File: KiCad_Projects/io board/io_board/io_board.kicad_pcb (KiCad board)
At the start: 2 copper layers, 78.4 x 100.1 mm, 15 parts, among them J1 Conn_01x13_Female, SW1 SW_Push, SW2 SW_Push, SW3 SW_Push, SW4 SW_Push, SW5 SW_DIP_x01, U1 LCD_Module

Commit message: 基盤データのアップデート
ローカルコミットはちゃんと作ってください
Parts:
- turned SW5 to -90 degrees
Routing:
- net GND1: track 49.0 -> 38.2 mm
- net +7.5V: track 45.2 -> 46.8 mm
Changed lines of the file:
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@@
   )
   (footprint "Lib:DS-850k" (layer "F.Cu")
-    (at 179.324 72.644 90)
+    (at 179.324 72.644 -90)
     (property "Sheetfile" "io_board.kicad_sch")
     (property "Sheetname" "")
@@
     (fp_line (start -10.5 -7.5) (end -10.5 7.5) (layer "F.SilkS") (width 0.12))
     (fp_line (start -7.5 4.7) (end 7.5 4.7) (layer "F.SilkS") (width 0.12))
-    (pad "1" thru_hole oval locked (at 0 0 180) (size 4 2) (drill oval 3 1) (layers *.Cu *.Mask)
+    (pad "1" thru_hole oval locked (at 0 0) (size 4 2) (drill oval 3 1) (layers *.Cu *.Mask)
       (net 13 "+7.5V") (pintype "passive"))
-    (pad "2" thru_hole oval locked (at -6 0 180) (size 4 2) (drill oval 3 1) (layers *.Cu *.Mask)
+    (pad "2" thru_hole oval locked (at -6 0) (size 4 2) (drill oval 3 1) (layers *.Cu *.Mask)
       (net 12 "GND1") (pintype "passive"))
   )
@@
   (segment (start 163.576 61.976) (end 169.672 68.072) (width 0.25) (layer "B.Cu") (net 11))
   (segment (start 141.239 54.879) (end 148.336 61.976) (width 0.25) (layer "B.Cu") (net 11))
-  (segment (start 153.939 52.817) (end 153.939 50.267) (width 2) (layer "B.Cu") (net 12))
-  (segment (start 172.292 71.612) (end 172.292 53.892978) (width 2) (layer "B.Cu") (net 12))
-  (segment (start 153.924 52.832) (end 153.939 52.817) (width 2) (layer "B.Cu") (net 12))
-  (segment (start 171.231022 52.832) (end 153.924 52.832) (width 2) (layer "B.Cu") (net 12))
-  (segment (start 179.324 78.644) (end 172.292 71.612) (width 2) (layer "B.Cu") (net 12))
-  (segment (start 172.292 53.892978) (end 171.231022 52.832) (width 2) (layer "B.Cu") (net 12))
-  (segment (start 179.299 50.267) (end 156.479 50.267) (width 2) (layer "B.Cu") (net 13))
-  (segment (start 179.324 72.644) (end 179.324 50.292) (width 2) (layer "B.Cu") (net 13))
-  (segment (start 179.324 50.292) (end 179.299 50.267) (width 2) (layer "B.Cu") (net 13))
+  (segment (start 154.686 52.832) (end 173.99 52.832) (width 2) (layer "B.Cu") (net 12))
+  (segment (start 153.939 52.085) (end 154.686 52.832) (width 2) (layer "B.Cu") (net 12))
+  (segment (start 153.939 50.267) (end 153.939 52.085) (width 2) (layer "B.Cu") (net 12))
+  (segment (start 179.324 58.166) (end 179.324 66.644) (width 2) (layer "B.Cu") (net 12))
+  (segment (start 173.99 52.832) (end 179.324 58.166) (width 2) (layer "B.Cu") (net 12))
+  (segment (start 156.479 50.267) (end 175.235 50.267) (width 2) (layer "B.Cu") (net 13))
+  (segment (start 175.235 50.267) (end 184.15 59.182) (width 2) (layer "B.Cu") (net 13))
+  (segment (start 184.15 59.182) (end 184.15 67.818) (width 2) (layer "B.Cu") (net 13))
+  (segment (start 184.15 67.818) (end 179.324 72.644) (width 2) (layer "B.Cu") (net 13))
   (group "" (id eb329cff-7bda-47da-8e95-d459de893e2d)
     (members

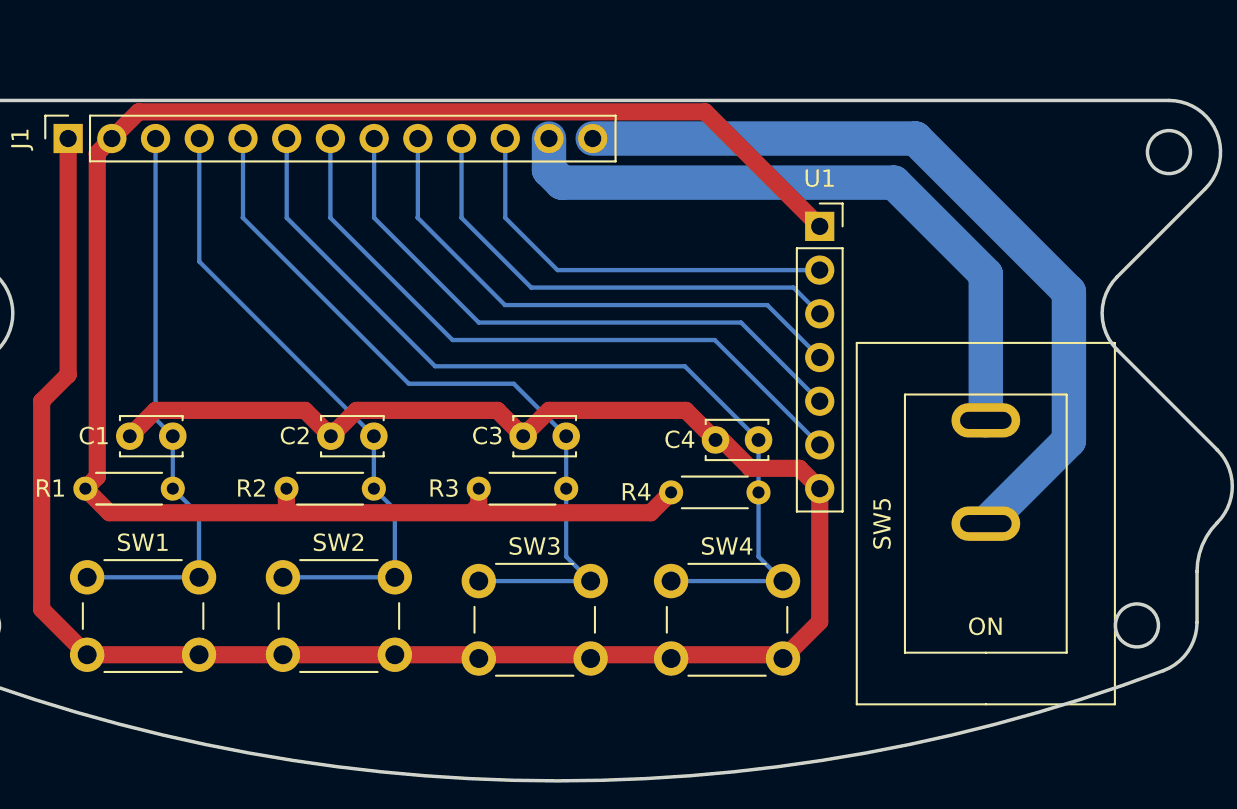
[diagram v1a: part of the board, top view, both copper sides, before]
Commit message: 基板データの更新
IO基板、ライン基板、電源基盤のコネクタ変更、最終確認
メイン基板制作中。
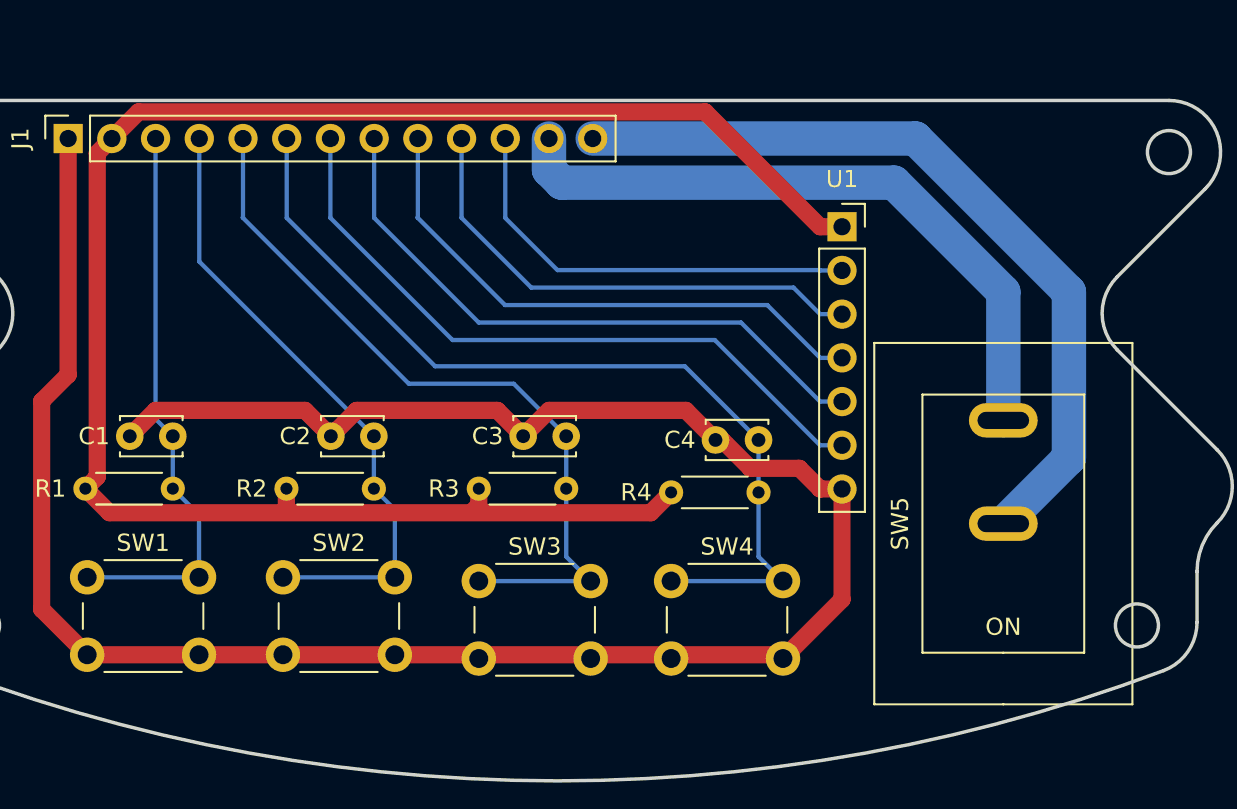
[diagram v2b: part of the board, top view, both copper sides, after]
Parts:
- moved U1 1.30 mm to (171.0, 55.4)
- moved SW5 1.02 mm to (180.3, 72.6)
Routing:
- net GND: track 169.5 -> 171.4 mm
- net +5V: track 139.6 -> 141.0 mm
- net SCLK: track 34.9 -> 36.2 mm
- net RS: track 31.3 -> 32.6 mm
- net RE: track 27.7 -> 29.0 mm
- net CS: track 24.1 -> 25.4 mm
- net SDI: track 38.5 -> 39.8 mm
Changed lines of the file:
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@@
   )
   (footprint "Connector_PinSocket_2.54mm:PinSocket_1x07_P2.54mm_Vertical" (layer "F.Cu")
-    (at 169.672 55.372)
+    (at 170.967 55.392)
     (descr "Through hole straight socket strip, 1x07, 2.54mm pitch, single row (from Kicad 4.0.7), script generated")
     (tags "Through hole socket strip THT 1x07 2.54mm single row")
@@
   )
   (footprint "Lib:DS-850k" (layer "F.Cu")
-    (at 179.324 72.644 -90)
+    (at 180.34 72.644 -90)
     (property "Sheetfile" "io_board.kicad_sch")
     (property "Sheetname" "")
@@
   (segment (start 150.940489 66.064489) (end 152.44 67.564) (width 1) (layer "F.Cu") (net 2))
   (segment (start 139.764489 66.064489) (end 141.264 67.564) (width 1) (layer "F.Cu") (net 2))
+  (segment (start 169.692 70.632) (end 168.490489 69.430489) (width 1) (layer "F.Cu") (net 2))
   (segment (start 163.616 67.782) (end 163.99537 67.782) (width 1) (layer "F.Cu") (net 2))
-  (segment (start 169.672 70.612) (end 169.672 78.346) (width 1) (layer "F.Cu") (net 2))
   (segment (start 125.999 50.267) (end 125.999 63.993) (width 1) (layer "F.Cu") (net 2))
-  (segment (start 169.672 78.346) (end 167.536 80.482) (width 1) (layer "F.Cu") (net 2))
   (segment (start 165.643859 69.430489) (end 168.490489 69.430489) (width 1) (layer "F.Cu") (net 2))
-  (segment (start 168.490489 69.430489) (end 169.672 70.612) (width 1) (layer "F.Cu") (net 2))
   (segment (start 125.999 50.267) (end 125.975489 50.290511) (width 0.25) (layer "F.Cu") (net 2))
   (segment (start 127.104 80.264) (end 133.604 80.264) (width 0.25) (layer "F.Cu") (net 2))
   (segment (start 129.58 67.564) (end 131.079511 66.064489) (width 1) (layer "F.Cu") (net 2))
+  (segment (start 170.967 70.632) (end 169.692 70.632) (width 1) (layer "F.Cu") (net 2))
   (segment (start 167.318 80.264) (end 167.536 80.482) (width 1) (layer "F.Cu") (net 2))
+  (segment (start 170.967 77.051) (end 170.967 70.632) (width 1) (layer "F.Cu") (net 2))
+  (segment (start 167.536 80.482) (end 170.967 77.051) (width 1) (layer "F.Cu") (net 2))
   (segment (start 153.939511 66.064489) (end 161.898489 66.064489) (width 1) (layer "F.Cu") (net 2))
   (segment (start 125.999 63.993) (end 124.46 65.532) (width 1) (layer "F.Cu") (net 2))
@@
   (segment (start 138.699 54.879) (end 138.699 50.267) (width 0.25) (layer "B.Cu") (net 5))
   (segment (start 167.536 75.982) (end 166.116 74.562) (width 0.25) (layer "B.Cu") (net 5))
-  (segment (start 163.017489 48.717489) (end 169.672 55.372) (width 1) (layer "F.Cu") (net 6))
   (segment (start 138.684 70.612) (end 138.684 71.573022) (width 1) (layer "F.Cu") (net 6))
-  (segment (start 128.539 50.267) (end 130.088511 48.717489) (width 1) (layer "F.Cu") (net 6))
+  (segment (start 130.088511 48.717489) (end 128.539 50.267) (width 1) (layer "F.Cu") (net 6))
   (segment (start 149.86 70.612) (end 149.86 71.628) (width 0.25) (layer "F.Cu") (net 6))
+  (segment (start 170.967 55.392) (end 169.692 55.392) (width 1) (layer "F.Cu") (net 6))
   (segment (start 138.402511 71.854511) (end 149.578511 71.854511) (width 0.25) (layer "F.Cu") (net 6))
   (segment (start 149.578511 71.854511) (end 150.086511 71.854511) (width 0.25) (layer "F.Cu") (net 6))
+  (segment (start 169.692 55.392) (end 163.017489 48.717489) (width 1) (layer "F.Cu") (net 6))
   (segment (start 128.399511 72.011511) (end 159.854489 72.011511) (width 1) (layer "F.Cu") (net 6))
   (segment (start 127.689 69.923) (end 127 70.612) (width 1) (layer "F.Cu") (net 6))
@@
   (segment (start 159.854489 72.011511) (end 161.036 70.83) (width 1) (layer "F.Cu") (net 6))
   (segment (start 160.011489 71.854511) (end 161.036 70.83) (width 0.25) (layer "F.Cu") (net 6))
+  (segment (start 163.017489 48.717489) (end 130.088511 48.717489) (width 1) (layer "F.Cu") (net 6))
   (segment (start 150.086511 71.854511) (end 160.011489 71.854511) (width 0.25) (layer "F.Cu") (net 6))
   (segment (start 138.684 71.573022) (end 138.402511 71.854511) (width 0.25) (layer "F.Cu") (net 6))
@@
   (segment (start 127 70.612) (end 128.399511 72.011511) (width 1) (layer "F.Cu") (net 6))
   (segment (start 127.689 51.117) (end 127.689 69.923) (width 1) (layer "F.Cu") (net 6))
-  (segment (start 130.088511 48.717489) (end 163.017489 48.717489) (width 1) (layer "F.Cu") (net 6))
   (segment (start 149.86 71.573022) (end 149.578511 71.854511) (width 1) (layer "F.Cu") (net 6))
   (segment (start 149.86 71.628) (end 150.086511 71.854511) (width 0.25) (layer "F.Cu") (net 6))
   (segment (start 127 70.612) (end 128.242511 71.854511) (width 0.25) (layer "F.Cu") (net 6))
+  (segment (start 169.672 57.912) (end 169.692 57.932) (width 0.25) (layer "B.Cu") (net 7))
   (segment (start 151.399 54.879) (end 154.432 57.912) (width 0.25) (layer "B.Cu") (net 7))
   (segment (start 154.432 57.912) (end 169.672 57.912) (width 0.25) (layer "B.Cu") (net 7))
+  (segment (start 170.967 57.932) (end 169.692 57.932) (width 0.25) (layer "B.Cu") (net 7))
   (segment (start 151.399 50.267) (end 151.399 54.879) (width 0.25) (layer "B.Cu") (net 7))
-  (segment (start 152.908 58.928) (end 168.148 58.928) (width 0.25) (layer "B.Cu") (net 8))
-  (segment (start 168.148 58.928) (end 169.672 60.452) (width 0.25) (layer "B.Cu") (net 8))
-  (segment (start 148.859 50.267) (end 148.859 54.879) (width 0.25) (layer "B.Cu") (net 8))
-  (segment (start 148.859 54.879) (end 152.908 58.928) (width 0.25) (layer "B.Cu") (net 8))
-  (segment (start 146.304 54.864) (end 151.384 59.944) (width 0.25) (layer "B.Cu") (net 9))
-  (segment (start 146.319 54.849) (end 146.304 54.864) (width 0.25) (layer "B.Cu") (net 9))
-  (segment (start 166.624 59.944) (end 169.672 62.992) (width 0.25) (layer "B.Cu") (net 9))
-  (segment (start 151.384 59.944) (end 166.624 59.944) (width 0.25) (layer "B.Cu") (net 9))
-  (segment (start 146.319 50.267) (end 146.319 54.849) (width 0.25) (layer "B.Cu") (net 9))
-  (segment (start 169.672 65.532) (end 165.1 60.96) (width 0.25) (layer "B.Cu") (net 10))
+  (segment (start 148.859 54.879) (end 148.859 50.267) (width 0.25) (layer "B.Cu") (net 8))
+  (segment (start 169.692 60.472) (end 168.148 58.928) (width 0.25) (layer "B.Cu") (net 8))
+  (segment (start 170.967 60.472) (end 169.692 60.472) (width 0.25) (layer "B.Cu") (net 8))
+  (segment (start 152.908 58.928) (end 148.859 54.879) (width 0.25) (layer "B.Cu") (net 8))
+  (segment (start 168.148 58.928) (end 152.908 58.928) (width 0.25) (layer "B.Cu") (net 8))
+  (segment (start 151.384 59.944) (end 146.304 54.864) (width 0.25) (layer "B.Cu") (net 9))
+  (segment (start 146.304 54.864) (end 146.319 54.849) (width 0.25) (layer "B.Cu") (net 9))
+  (segment (start 166.624 59.944) (end 151.384 59.944) (width 0.25) (layer "B.Cu") (net 9))
+  (segment (start 146.319 54.849) (end 146.319 50.267) (width 0.25) (layer "B.Cu") (net 9))
+  (segment (start 170.967 63.012) (end 169.692 63.012) (width 0.25) (layer "B.Cu") (net 9))
+  (segment (start 169.692 63.012) (end 166.624 59.944) (width 0.25) (layer "B.Cu") (net 9))
+  (segment (start 170.967 65.552) (end 169.692 65.552) (width 0.25) (layer "B.Cu") (net 10))
+  (segment (start 149.86 60.96) (end 143.779 54.879) (width 0.25) (layer "B.Cu") (net 10))
+  (segment (start 169.692 65.552) (end 165.1 60.96) (width 0.25) (layer "B.Cu") (net 10))
+  (segment (start 165.1 60.96) (end 149.86 60.96) (width 0.25) (layer "B.Cu") (net 10))
   (segment (start 143.779 54.879) (end 143.779 50.267) (width 0.25) (layer "B.Cu") (net 10))
-  (segment (start 149.86 60.96) (end 143.779 54.879) (width 0.25) (layer "B.Cu") (net 10))
-  (segment (start 165.1 60.96) (end 149.86 60.96) (width 0.25) (layer "B.Cu") (net 10))
-  (segment (start 148.336 61.976) (end 163.576 61.976) (width 0.25) (layer "B.Cu") (net 11))
-  (segment (start 141.239 50.267) (end 141.239 54.879) (width 0.25) (layer "B.Cu") (net 11))
-  (segment (start 163.576 61.976) (end 169.672 68.072) (width 0.25) (layer "B.Cu") (net 11))
-  (segment (start 141.239 54.879) (end 148.336 61.976) (width 0.25) (layer "B.Cu") (net 11))
-  (segment (start 154.686 52.832) (end 173.99 52.832) (width 2) (layer "B.Cu") (net 12))
-  (segment (start 153.939 52.085) (end 154.686 52.832) (width 2) (layer "B.Cu") (net 12))
-  (segment (start 153.939 50.267) (end 153.939 52.085) (width 2) (layer "B.Cu") (net 12))
-  (segment (start 179.324 58.166) (end 179.324 66.644) (width 2) (layer "B.Cu") (net 12))
-  (segment (start 173.99 52.832) (end 179.324 58.166) (width 2) (layer "B.Cu") (net 12))
+  (segment (start 163.576 61.976) (end 148.336 61.976) (width 0.25) (layer "B.Cu") (net 11))
+  (segment (start 169.692 68.092) (end 163.576 61.976) (width 0.25) (layer "B.Cu") (net 11))
+  (segment (start 170.967 68.092) (end 169.692 68.092) (width 0.25) (layer "B.Cu") (net 11))
+  (segment (start 141.239 54.879) (end 141.239 50.267) (width 0.25) (layer "B.Cu") (net 11))
+  (segment (start 148.336 61.976) (end 141.239 54.879) (width 0.25) (layer "B.Cu") (net 11))
+  (segment (start 180.34 66.644) (end 180.34 59.182) (width 2) (layer "B.Cu") (net 12))
+  (segment (start 153.939 52.085) (end 153.939 50.267) (width 2) (layer "B.Cu") (net 12))
+  (segment (start 154.686 52.832) (end 153.939 52.085) (width 2) (layer "B.Cu") (net 12))
+  (segment (start 173.99 52.832) (end 154.686 52.832) (width 2) (layer "B.Cu") (net 12))
+  (segment (start 180.34 59.182) (end 173.99 52.832) (width 2) (layer "B.Cu") (net 12))
+  (segment (start 184.15 59.182) (end 184.15 68.834) (width 2) (layer "B.Cu") (net 13))
   (segment (start 156.479 50.267) (end 175.235 50.267) (width 2) (layer "B.Cu") (net 13))
   (segment (start 175.235 50.267) (end 184.15 59.182) (width 2) (layer "B.Cu") (net 13))
-  (segment (start 184.15 59.182) (end 184.15 67.818) (width 2) (layer "B.Cu") (net 13))
-  (segment (start 184.15 67.818) (end 179.324 72.644) (width 2) (layer "B.Cu") (net 13))
+  (segment (start 184.15 68.834) (end 180.34 72.644) (width 2) (layer "B.Cu") (net 13))
   (group "" (id eb329cff-7bda-47da-8e95-d459de893e2d)
     (members
